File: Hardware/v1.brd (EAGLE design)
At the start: 50 x 40 mm, 79 parts, among them IC1 LM324D, IC2 m328p, IC3 REG1117, J1 22-27-2061-06, J2 22-27-2021-02, J3 22-27-2021-02, J4 22-27-2031-03, J5 22-27-2041-04, Q1 BSS123, Q2 BSS123, Q3 BSS123, Q5 BSS123

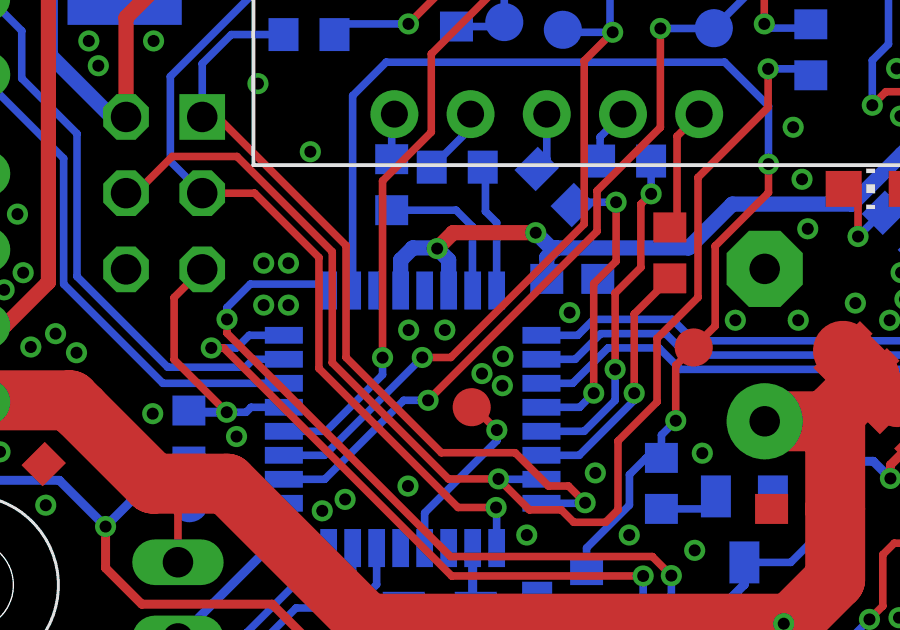
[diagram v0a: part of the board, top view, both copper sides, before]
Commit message: Added a 100nF cap to AREF (see issue #4). Added an extra LED to see if 5V is supplied.
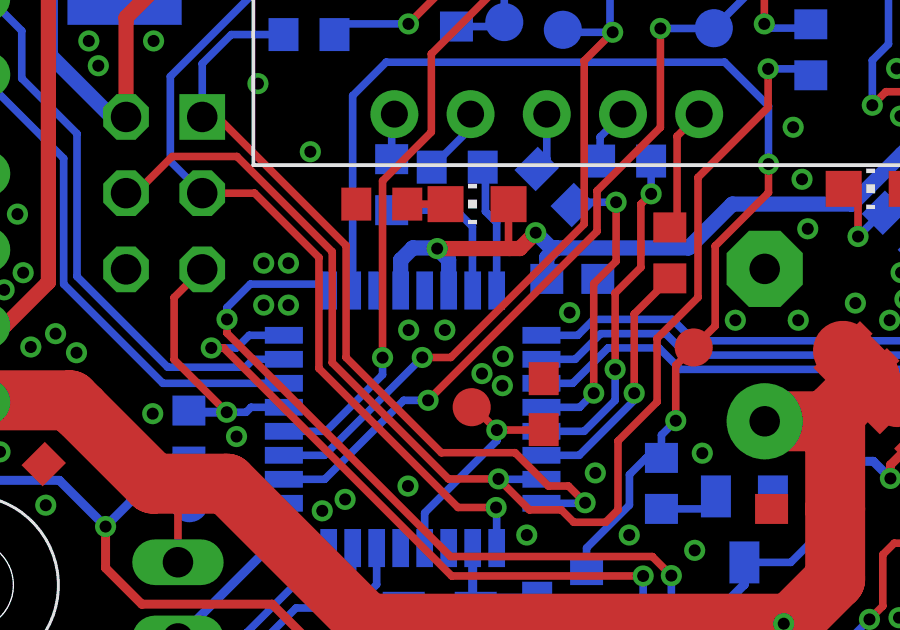
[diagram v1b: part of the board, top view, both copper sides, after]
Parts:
- added C17: 100n, rcl:C0603
- added LED2: GN, led:CHIP-LED0805
- added R29: 280, rcl:R0603
- LED1: value (none) -> RD
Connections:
- new net N$24: LED2.C, R29.2
- net AREF: now also C17.2
- net GND: now also C17.1, R29.1
- net VCC: now also LED2.A
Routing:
- net AREF: track 6.08 -> 7.66 mm
- net VCC: track 145.1 -> 146.6 mm
- net N$24: track 0.00 -> 1.28 mm
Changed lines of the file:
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@@
 <?xml version="1.0" encoding="utf-8"?>
 <!DOCTYPE eagle SYSTEM "eagle.dtd">
-<eagle version="6.5.0">
+<eagle version="7.2.0">
 <drawing>
 <settings>
@@
 <pass name="Default">
 <param name="RoutingGrid" value="3.125mil"/>
+<param name="AutoGrid" value="1"/>
+<param name="Efforts" value="0"/>
+<param name="TopRouterVariant" value="1"/>
 <param name="tpViaShape" value="round"/>
 <param name="PrefDir.1" value="|"/>
@@
 <attribute name="VALUE" x="20.1422" y="9.1694" size="0.0254" layer="27"/>
 </element>
-<element name="LED1" library="led" package="CHIP-LED0805" value="" x="34.2265" y="17.2085" smashed="yes" rot="R90">
+<element name="LED1" library="led" package="CHIP-LED0805" value="RD" x="34.2265" y="17.2085" smashed="yes" rot="R90">
 <attribute name="NAME" x="32.39010625" y="16.256590625" size="1.143" layer="33" font="vector" ratio="15" rot="R90"/>
 <attribute name="VALUE" x="36.226503125" y="16.208496875" size="1.27" layer="27" rot="R90"/>
@@
 <element name="R28" library="rcl" package="R0603" value="n.m." x="11.2395" y="35.6235" smashed="yes">
 <attribute name="NAME" x="10.414" y="34.798" size="1.143" layer="33" font="vector" ratio="15" rot="R180"/>
+</element>
+<element name="C17" library="rcl" package="C0603" value="100n" x="23.1775" y="10.033" smashed="yes" rot="R270">
+<attribute name="NAME" x="21.717" y="11.7475" size="1.143" layer="33" font="vector" ratio="15"/>
+</element>
+<element name="LED2" library="led" package="CHIP-LED0805" value="GN" x="20.955" y="16.7005" smashed="yes" rot="R90">
+<attribute name="NAME" x="24.0665" y="15.8115" size="1.143" layer="33" font="vector" ratio="15" rot="R180"/>
+</element>
+<element name="R29" library="rcl" package="R0603" value="280" x="17.78" y="16.7005" smashed="yes">
+<attribute name="NAME" x="16.1925" y="14.859" size="1.143" layer="33" font="vector" ratio="15" rot="R90"/>
 </element>
 </elements>
@@
 <wire x1="35.1075625" y1="18.3594375" x2="33.448625" y2="16.7005" width="0.508" layer="16"/>
 <via x="19.626571875" y="15.219053125" extent="1-16" drill="0.4"/>
-<wire x1="19.626571875" y1="15.219053125" x2="20.15551875" y2="15.748" width="0.508" layer="1"/>
-<wire x1="20.15551875" y1="15.748" x2="22.9108" y2="15.748" width="0.508" layer="1"/>
 <via x="22.9108" y="15.748" extent="1-16" drill="0.4"/>
 <wire x1="22.9108" y1="15.748" x2="23.4188" y2="15.24" width="0.508" layer="16"/>
@@
 <wire x1="8.5725" y1="5.953125" x2="10.73875" y2="8.119375" width="0.3" layer="16"/>
 <wire x1="10.73875" y1="8.119375" x2="11.350625" y2="8.119375" width="0.3" layer="16"/>
+<contactref element="LED2" pad="A"/>
+<wire x1="22.005" y1="15.248553125" x2="22.005" y2="16.7005" width="0.254" layer="1"/>
+<wire x1="19.626571875" y1="15.219053125" x2="22.0345" y2="15.219053125" width="0.508" layer="1"/>
+<wire x1="22.0345" y1="15.219053125" x2="22.381853125" y2="15.219053125" width="0.508" layer="1"/>
+<wire x1="22.381853125" y1="15.219053125" x2="22.9108" y2="15.748" width="0.508" layer="1"/>
+<wire x1="22.005" y1="15.248553125" x2="22.0345" y2="15.219053125" width="0.254" layer="1"/>
 </signal>
 <signal name="GND">
@@
 <wire x1="22.958425" y1="1.864625" x2="23.17205" y2="1.651" width="0.4064" layer="16"/>
 <wire x1="23.17205" y1="1.651" x2="24.5745" y2="1.651" width="0.4064" layer="16"/>
+<contactref element="C17" pad="1"/>
+<contactref element="R29" pad="1"/>
 </signal>
 <signal name="N$1">
@@
 <wire x1="20.7772" y1="9.9314" x2="20.8788" y2="9.8298" width="0.254" layer="1"/>
 <wire x1="20.8788" y1="9.8298" x2="20.955" y2="9.8298" width="0.254" layer="1"/>
+<contactref element="C17" pad="2"/>
+<wire x1="21.6154" y1="9.1694" x2="23.1775" y2="9.1694" width="0.254" layer="1"/>
+<wire x1="23.1775" y1="9.1694" x2="23.1775" y2="9.183" width="0.254" layer="1"/>
 </signal>
 <signal name="N$25">
@@
 <wire x1="8.9535" y1="35.6235" x2="10.3895" y2="35.6235" width="0.3" layer="1"/>
 </signal>
+<signal name="N$24">
+<contactref element="LED2" pad="C"/>
+<contactref element="R29" pad="2"/>
+<wire x1="19.905" y1="16.7005" x2="18.63" y2="16.7005" width="0.254" layer="1"/>
+</signal>
 </signals>

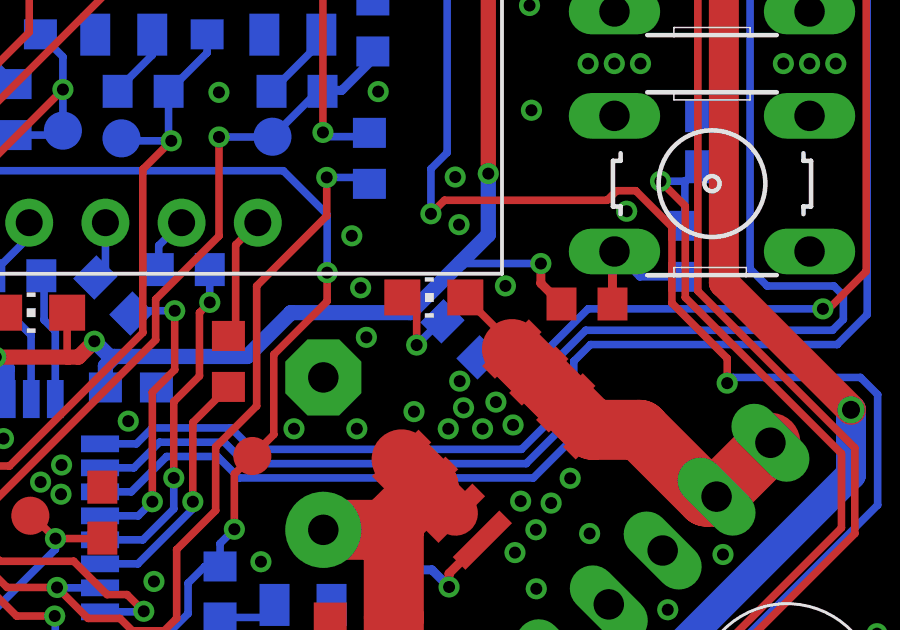
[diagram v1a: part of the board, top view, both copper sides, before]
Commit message: Changed resistors at the LED display to 300 Ohm to reduce power drain under 5V supply. Changed the position of the LED showing the duty cycle of the p-fet slightly to make it easier to solder it on.
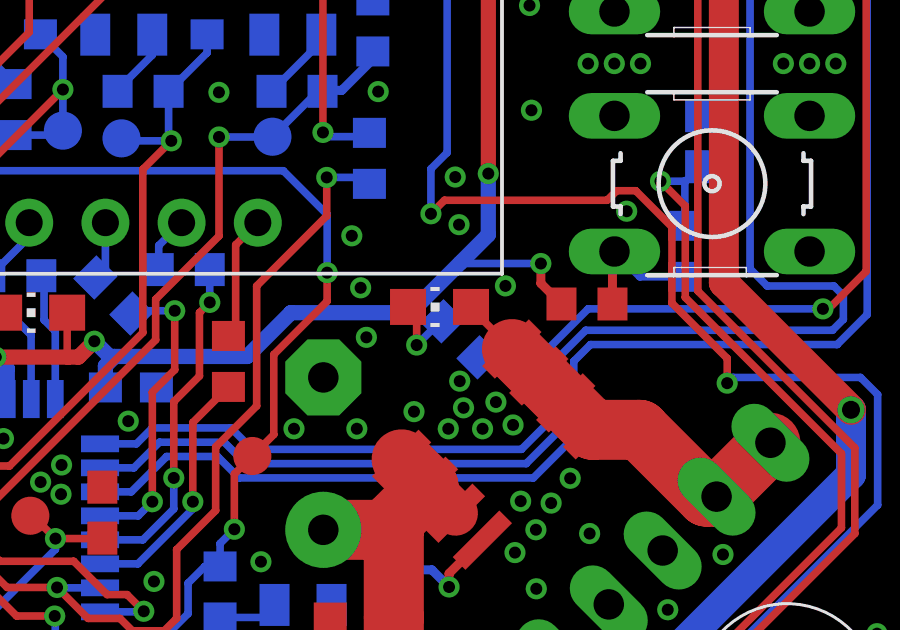
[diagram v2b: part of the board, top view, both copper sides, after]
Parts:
- R10, R11, R12, R13, R14, R3, R4, R8: value 150 -> 300
- moved LED1 0.37 mm to (34.4, 16.9)
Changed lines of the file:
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@@
 <attribute name="NAME" x="19.3802" y="35.4076" size="1.143" layer="33" font="vector" ratio="15"/>
 </element>
-<element name="R3" library="rcl" package="R0603" value="150" x="16.5608" y="24.0792" smashed="yes" rot="MR0">
+<element name="R3" library="rcl" package="R0603" value="300" x="16.5608" y="24.0792" smashed="yes" rot="MR0">
 <attribute name="NAME" x="14.9098" y="23.5712" size="1.143" layer="34" font="vector" ratio="15" rot="MR0"/>
 </element>
-<element name="R4" library="rcl" package="R0603" value="150" x="32.0802" y="21.844" smashed="yes" rot="MR270">
+<element name="R4" library="rcl" package="R0603" value="300" x="32.0802" y="21.844" smashed="yes" rot="MR270">
 <attribute name="NAME" x="34.1757" y="22.5425" size="1.143" layer="34" font="vector" ratio="15" rot="MR270"/>
 </element>
-<element name="R8" library="rcl" package="R0603" value="150" x="15.3543" y="22.352" smashed="yes" rot="MR0">
+<element name="R8" library="rcl" package="R0603" value="300" x="15.3543" y="22.352" smashed="yes" rot="MR0">
 <attribute name="NAME" x="16.4338" y="20.32" size="1.143" layer="34" font="vector" ratio="15" rot="MR0"/>
 </element>
-<element name="R10" library="rcl" package="R0603" value="150" x="27.3812" y="15.0749" smashed="yes" rot="R270">
+<element name="R10" library="rcl" package="R0603" value="300" x="27.3812" y="15.0749" smashed="yes" rot="R270">
 <attribute name="NAME" x="25.3492" y="16.7894" size="1.143" layer="33" font="vector" ratio="15" rot="R270"/>
 </element>
-<element name="R11" library="rcl" package="R0603" value="150" x="18.1102" y="17.3482" smashed="yes" rot="MR270">
+<element name="R11" library="rcl" package="R0603" value="300" x="18.1102" y="17.3482" smashed="yes" rot="MR270">
 <attribute name="NAME" x="17.3482" y="19.1262" size="1.143" layer="34" font="vector" ratio="15" rot="MR270"/>
 </element>
-<element name="R12" library="rcl" package="R0603" value="150" x="25.908" y="18.1356" smashed="yes" rot="MR180">
+<element name="R12" library="rcl" package="R0603" value="300" x="25.908" y="18.1356" smashed="yes" rot="MR180">
 <attribute name="NAME" x="25.0825" y="17.5006" size="1.143" layer="34" font="vector" ratio="15" rot="MR180"/>
 </element>
-<element name="R13" library="rcl" package="R0603" value="150" x="20.2946" y="17.9324" smashed="yes" rot="MR180">
+<element name="R13" library="rcl" package="R0603" value="300" x="20.2946" y="17.9324" smashed="yes" rot="MR180">
 <attribute name="NAME" x="21.7424" y="16.0401" size="1.143" layer="34" font="vector" ratio="15" rot="MR0"/>
 </element>
-<element name="R14" library="rcl" package="R0603" value="150" x="23.5458" y="17.272" smashed="yes" rot="MR225">
+<element name="R14" library="rcl" package="R0603" value="300" x="23.5458" y="17.272" smashed="yes" rot="MR225">
 <attribute name="NAME" x="24.405725" y="16.129003125" size="1.143" layer="34" font="vector" ratio="15" rot="MR180"/>
 </element>
@@
 <attribute name="VALUE" x="20.1422" y="9.1694" size="0.0254" layer="27"/>
 </element>
-<element name="LED1" library="led" package="CHIP-LED0805" value="RD" x="34.2265" y="17.2085" smashed="yes" rot="R90">
-<attribute name="NAME" x="32.39010625" y="16.256590625" size="1.143" layer="33" font="vector" ratio="15" rot="R90"/>
-<attribute name="VALUE" x="36.226503125" y="16.208496875" size="1.27" layer="27" rot="R90"/>
+<element name="LED1" library="led" package="CHIP-LED0805" value="RD" x="34.417" y="16.891" smashed="yes" rot="R90">
+<attribute name="NAME" x="32.58060625" y="15.939090625" size="1.143" layer="33" font="vector" ratio="15" rot="R90"/>
+<attribute name="VALUE" x="36.417003125" y="15.890996875" size="1.27" layer="27" rot="R90"/>
 </element>
 <element name="R26" library="rcl" package="R0603" value="1k" x="35.1155" y="15.8115" smashed="yes" rot="MR45">
@@
 <wire x1="43.316025" y1="10.568075" x2="43.651578125" y2="10.568075" width="2" layer="1"/>
 <wire x1="45.447628125" y1="12.364125" x2="43.651578125" y2="10.568075" width="2" layer="1"/>
-<wire x1="35.2765" y1="17.2085" x2="36.8293125" y2="15.6556875" width="0.254" layer="1"/>
-<wire x1="36.8293125" y1="15.6556875" x2="36.8293125" y2="15.488640625" width="0.254" layer="1"/>
+<wire x1="35.467" y1="16.891" x2="35.467" y2="16.850953125" width="0.254" layer="1"/>
+<wire x1="35.467" y1="16.850953125" x2="36.8293125" y2="15.488640625" width="0.254" layer="1"/>
 </signal>
 <signal name="LCD_D">
@@
 <wire x1="33.655" y1="15.621" x2="34.446540625" y2="16.412540625" width="0.254" layer="16"/>
 <wire x1="34.446540625" y1="16.412540625" x2="34.514459375" y2="16.412540625" width="0.254" layer="16"/>
-<wire x1="33.1765" y1="17.2085" x2="33.655" y2="16.73" width="0.254" layer="1"/>
-<wire x1="33.655" y1="16.73" x2="33.655" y2="15.621" width="0.254" layer="1"/>
+<wire x1="33.655" y1="15.621" x2="33.655" y2="16.603" width="0.254" layer="1"/>
+<wire x1="33.655" y1="16.603" x2="33.367" y2="16.891" width="0.254" layer="1"/>
 </signal>
 <signal name="ADC7">

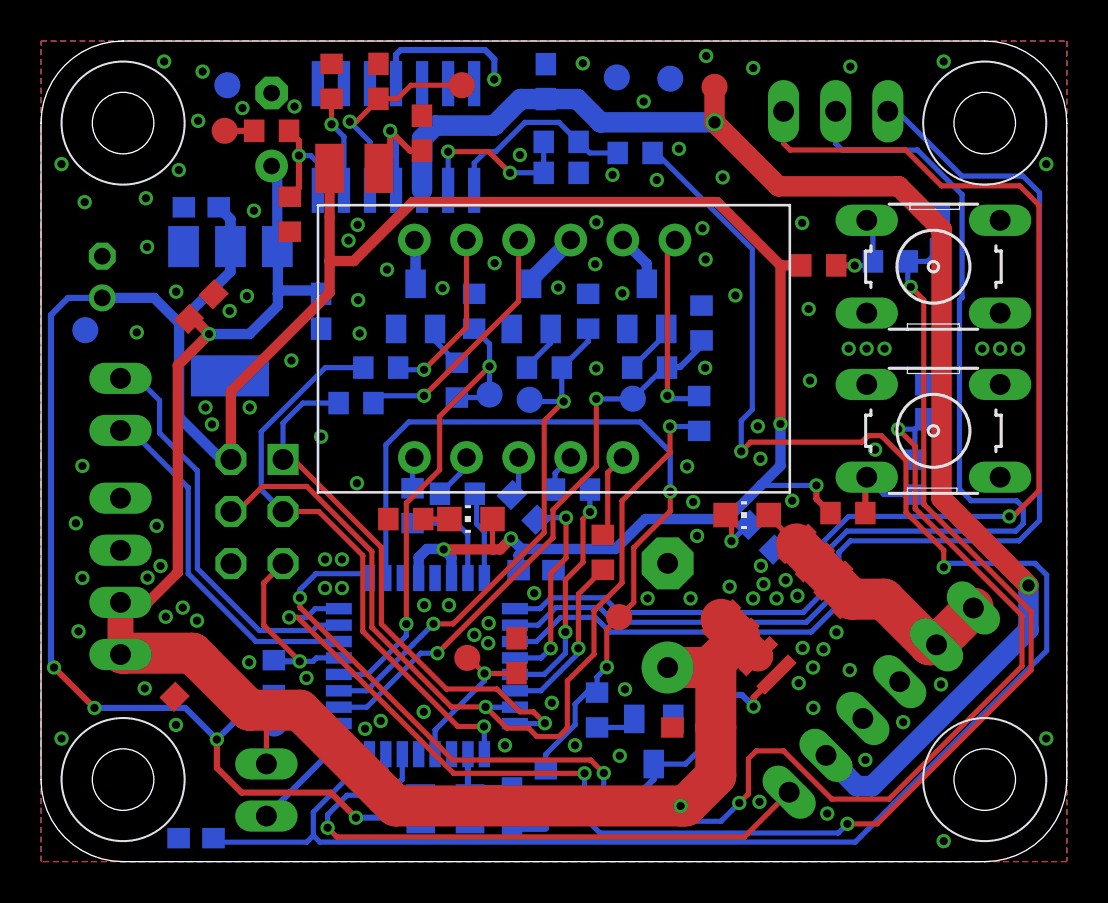
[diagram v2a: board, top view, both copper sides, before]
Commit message: Some minor changes to solve issues with overlapping components (especially smd components under polarized capacitors).
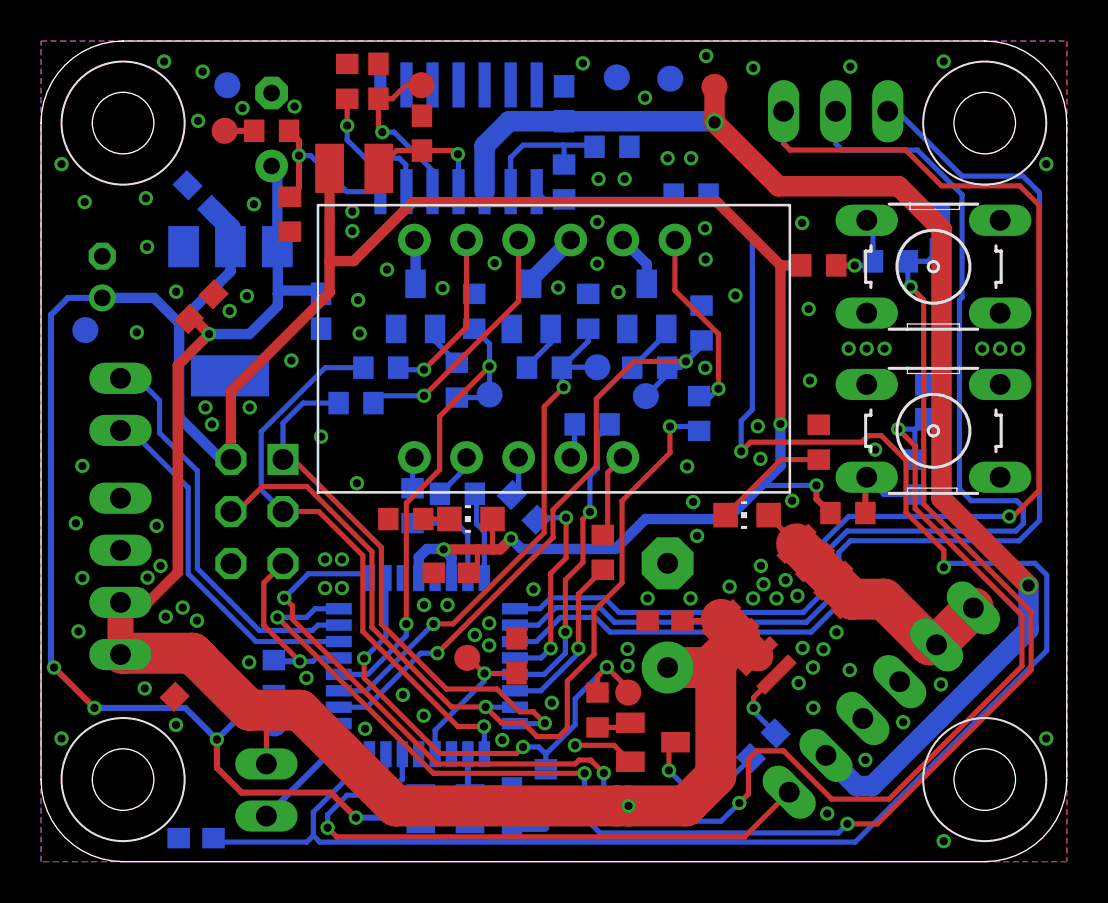
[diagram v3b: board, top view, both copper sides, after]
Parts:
- moved R26 5.41 mm to (37.9, 20.4), flipped to the top, turned to 270 degrees
- moved C12 5.34 mm to (30.4, 11.7)
- moved C8 4.13 mm to (20.0, 14.1), flipped to the top
- moved TP5 3.71 mm to (28.6, 8.24)
- moved TP2 3.66 mm to (27.1, 24.1)
- moved R27 3.40 mm to (31.7, 32.5)
- moved R12 3.31 mm to (26.9, 21.3)
- moved IC1 3.05 mm to (20.4, 35.3)
- moved R2 2.78 mm to (27.8, 34.8)
- moved R15 2.67 mm to (35.2, 5.65), turned to 315 degrees
- moved TP11 1.97 mm to (18.5, 37.8)
- moved R1 1.96 mm to (25.5, 33.1), turned to 270 degrees
- moved R36 1.40 mm to (31.1, 3.03), turned to 0 degrees
- moved C1 1.40 mm to (25.5, 36.9)
- moved R25 0.76 mm to (14.9, 38.0)
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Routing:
- net LOETKOLBEN_0: track 39.7 -> 25.3 mm, vias 2 -> 3
- net GND: track 9.18 -> 4.74 mm, vias 122 -> 117
- net SENSOR0: track 67.9 -> 63.8 mm
- net LCD_F: track 11.4 -> 14.9 mm
- net THERMO0: track 91.9 -> 88.7 mm
- net N$2: track 28.0 -> 31.2 mm
- net N$25: track 2.58 -> 5.66 mm, vias 1 -> 0
- net SDFGHJK: track 9.76 -> 6.93 mm
- net 12V: track 82.2 -> 84.7 mm
- net N$26: track 6.01 -> 8.30 mm
- net N$20: track 4.71 -> 6.69 mm
- net N$30: track 9.97 -> 8.36 mm
- net BUTTON_-: track 68.4 -> 70.0 mm
- net N$1: track 8.48 -> 6.99 mm, vias 2 -> 0
- net N$32: track 6.16 -> 6.98 mm, vias 0 -> 1
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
